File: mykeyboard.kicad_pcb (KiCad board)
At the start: 2 copper layers, 85.6 x 54 mm, 33 parts, among them J1 MJ-4PP-9, J2 LED, SW1 SW_PUSH, SW2 SW_PUSH, SW3 SW_PUSH, SW4 SW_PUSH, SW5 SW_PUSH, SW6 SW_PUSH, SW7 SW_PUSH, SW8 SW_PUSH, SW9 SW_PUSH, U1 ProMicro

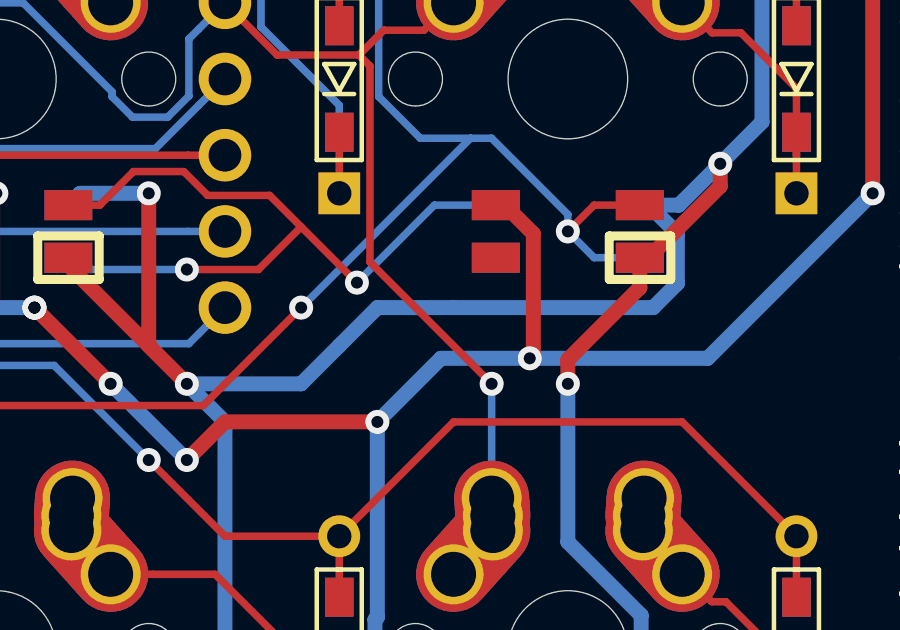
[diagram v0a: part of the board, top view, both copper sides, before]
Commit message: SW5 の LED が結線できていなかったのを修正
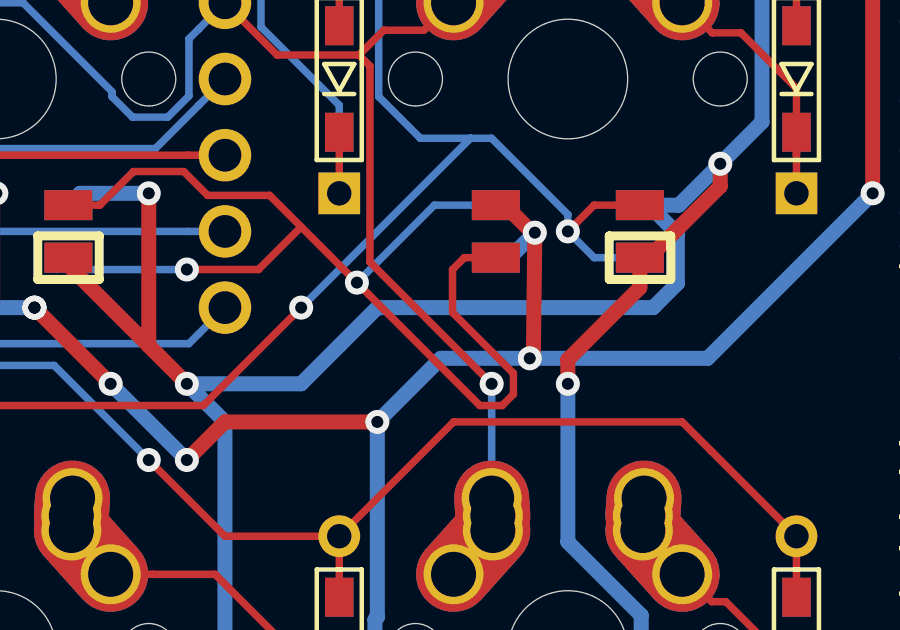
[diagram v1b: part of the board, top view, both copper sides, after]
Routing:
- net Net-(L5-Pad3): track 26.7 -> 40.4 mm
- net GND: track 279.6 -> 281.4 mm, vias 18 -> 19
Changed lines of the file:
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@@
     (thickness 1.6)
     (drawings 10)
-    (tracks 715)
+    (tracks 728)
     (zones 0)
     (modules 33)
@@
   )
   (setup
-    (last_trace_width 0.25)
+    (last_trace_width 0.5)
     (user_trace_width 0.5)
     (trace_clearance 0.2)
@@
   (via (at 173.99 105.829999) (size 0.8) (drill 0.4) (layers F.Cu B.Cu) (net 14))
   (segment (start 174.110001 105.709998) (end 173.99 105.829999) (width 0.5) (layer F.Cu) (net 14))
-  (segment (start 174.110001 101.675001) (end 174.110001 105.709998) (width 0.5) (layer F.Cu) (net 14))
   (segment (start 173.99 105.829999) (end 171.030001 105.829999) (width 0.5) (layer B.Cu) (net 14))
   (segment (start 179.920001 105.829999) (end 173.99 105.829999) (width 0.5) (layer B.Cu) (net 14))
@@
   (segment (start 128.663701 77.863701) (end 129.54 78.74) (width 0.5) (layer F.Cu) (net 14))
   (segment (start 119.46 80.01) (end 119.46 78.772564) (width 0.5) (layer F.Cu) (net 14))
+  (via (at 174.159233 101.64218) (size 0.8) (drill 0.4) (layers F.Cu B.Cu) (net 14))
+  (segment (start 174.159233 101.64218) (end 174.110001 105.709998) (width 0.5) (layer F.Cu) (net 14))
+  (segment (start 173.326413 102.475) (end 174.159233 101.64218) (width 0.5) (layer B.Cu) (net 14))
+  (segment (start 172.86 102.475) (end 173.326413 102.475) (width 0.5) (layer B.Cu) (net 14))
+  (segment (start 174.110001 101.675001) (end 174.159233 101.64218) (width 0.5) (layer F.Cu) (net 14))
   (segment (start 130.416299 85.483701) (end 129.54 86.36) (width 0.25) (layer B.Cu) (net 15))
   (segment (start 130.878699 85.021301) (end 130.416299 85.483701) (width 0.25) (layer B.Cu) (net 15))
@@
   (segment (start 159.005 102.87) (end 158.61 102.475) (width 0.25) (layer B.Cu) (net 37))
   (segment (start 162.56 102.87) (end 159.005 102.87) (width 0.25) (layer B.Cu) (net 37))
+  (segment (start 168.628734 103.70657) (end 168.228735 103.306571) (width 0.25) (layer F.Cu) (net 37))
+  (segment (start 172.327165 107.405001) (end 168.628734 103.70657) (width 0.25) (layer F.Cu) (net 37))
+  (segment (start 173.068001 107.405001) (end 172.327165 107.405001) (width 0.25) (layer F.Cu) (net 37))
+  (segment (start 173.445001 107.028001) (end 173.068001 107.405001) (width 0.25) (layer F.Cu) (net 37))
+  (segment (start 173.445001 106.331999) (end 173.445001 107.028001) (width 0.25) (layer F.Cu) (net 37))
+  (segment (start 171.415 102.87) (end 171.415 104.301998) (width 0.25) (layer F.Cu) (net 37))
+  (segment (start 171.81 102.475) (end 171.415 102.87) (width 0.25) (layer F.Cu) (net 37))
+  (segment (start 171.415 104.301998) (end 173.445001 106.331999) (width 0.25) (layer F.Cu) (net 37))
+  (segment (start 172.86 102.475) (end 171.81 102.475) (width 0.25) (layer F.Cu) (net 37))
   (segment (start 176.61 121.525) (end 175.735 120.65) (width 0.25) (layer B.Cu) (net 38))
   (segment (start 177.66 121.525) (end 176.61 121.525) (width 0.25) (layer B.Cu) (net 38))
